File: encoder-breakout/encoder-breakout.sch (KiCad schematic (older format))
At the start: 9 parts, among them J1 Conn_01x06_Female, U1 AEDR-8300

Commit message: Update encoder with 3d footprint
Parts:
- H1, H2: value MountingHole_Pad -> 9774060482R
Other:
- note removed: "TODO: choose correct mounting holes or smd screw receptacle"
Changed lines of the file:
@@
 EESchema Schematic File Version 4
+LIBS:encoder-breakout-cache
 EELAYER 30 0
 EELAYER END
@@
 P 5400 1850
 F 0 "H2" H 5500 1899 50  0000 L CNN
-F 1 "MountingHole_Pad" H 5500 1808 50  0000 L CNN
+F 1 "9774060482R" H 5500 1808 50  0000 L CNN
 F 2 "Jitter_Footprints:MountingHole_M4_threaded_6mm" H 5400 1850 50  0001 C CNN
-F 3 "~" H 5400 1850 50  0001 C CNN
+F 3 "http://www.farnell.com/datasheets/2580475.pdf" H 5400 1850 50  0001 C CNN
 	1    5400 1850
 	1    0    0    -1
@@
 	1    0    0    -1
 $EndComp
-Text Notes 3450 1550 0    79   ~ 0
-TODO: choose correct mounting holes or smd screw receptacle
 $Comp
 L Mechanical:MountingHole_Pad H1
@@
 P 4400 1850
 F 0 "H1" H 4500 1899 50  0000 L CNN
-F 1 "MountingHole_Pad" H 4500 1808 50  0000 L CNN
+F 1 "9774060482R" H 4500 1808 50  0000 L CNN
 F 2 "Jitter_Footprints:MountingHole_M4_threaded_6mm" H 4400 1850 50  0001 C CNN
-F 3 "~" H 4400 1850 50  0001 C CNN
+F 3 "http://www.farnell.com/datasheets/2580475.pdf" H 4400 1850 50  0001 C CNN
 	1    4400 1850
 	1    0    0    -1

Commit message: Add LED MPN information. add power led to UART board
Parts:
- D1: value LED -> KPT-1608EC; Farnell (none) -> 2099221
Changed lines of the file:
@@
 P 8650 1950
 F 0 "D1" V 8689 1833 50  0000 R CNN
-F 1 "LED" V 8598 1833 50  0000 R CNN
+F 1 "KPT-1608EC" V 8598 1833 50  0000 R CNN
 F 2 "LED_SMD:LED_0603_1608Metric" H 8650 1950 50  0001 C CNN
-F 3 "~" H 8650 1950 50  0001 C CNN
+F 3 "http://www.farnell.com/datasheets/2045911.pdf" H 8650 1950 50  0001 C CNN
+F 4 "2099221" V 8650 1950 50  0001 C CNN "Farnell"
 	1    8650 1950
 	0    -1   -1   0

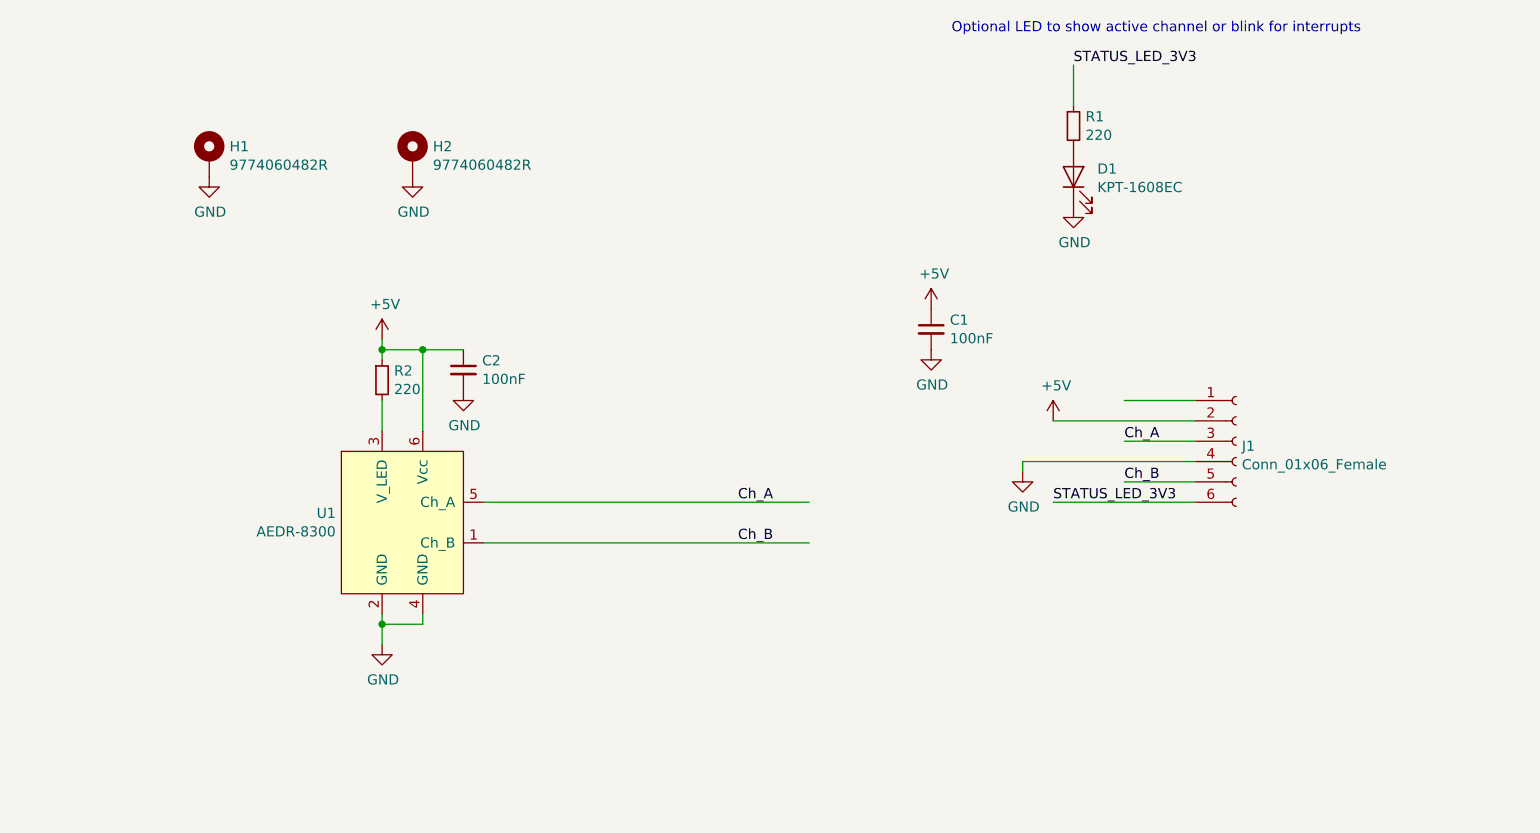
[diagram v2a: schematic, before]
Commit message: Fix schematics compile errors
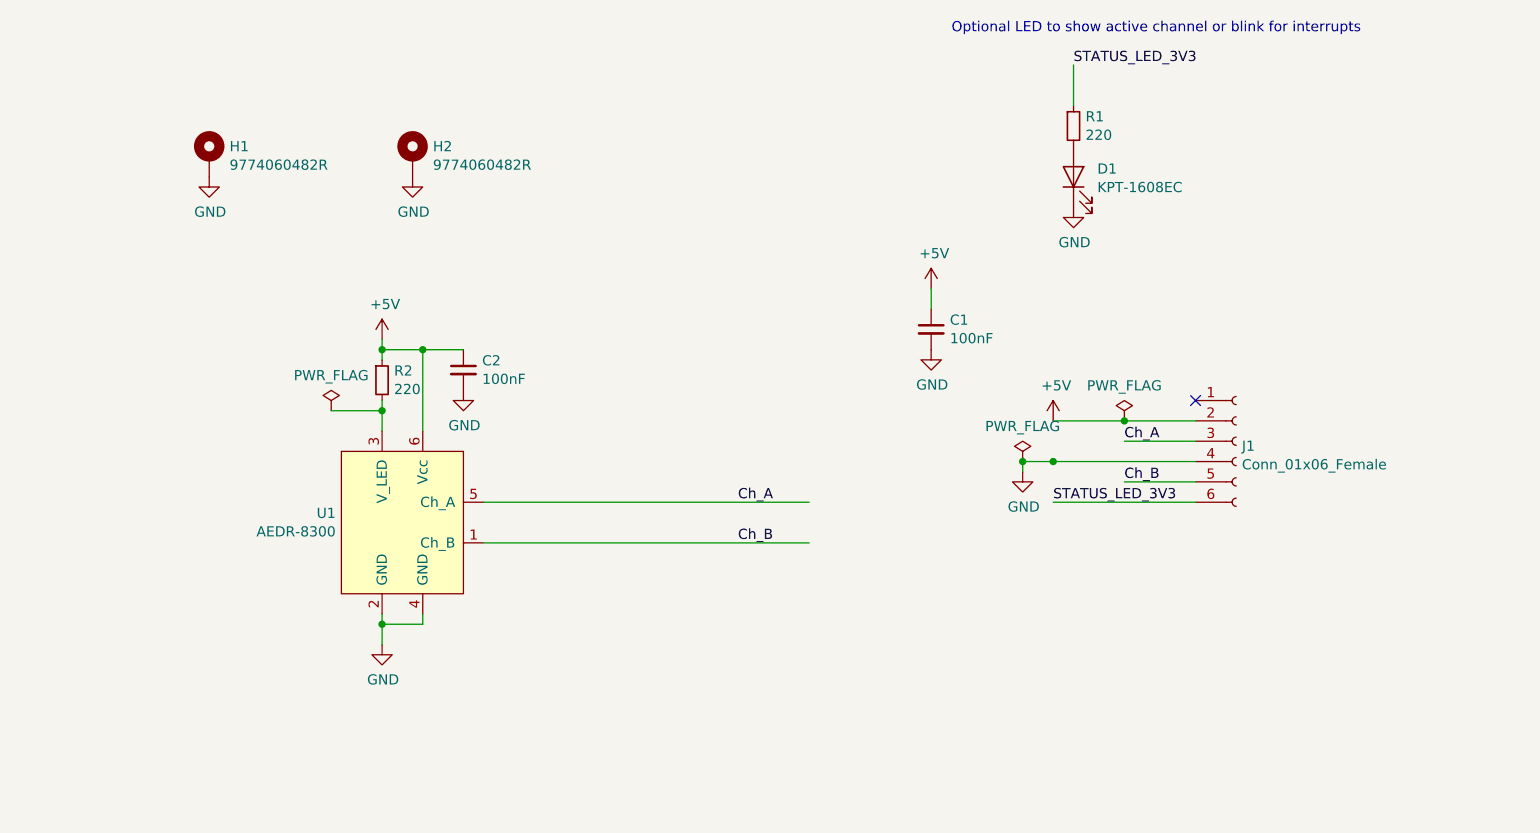
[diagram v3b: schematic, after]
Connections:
- wire segments 20 -> 24
- no-connect marks 0 -> 1
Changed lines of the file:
@@
 $EndComp
 Wire Wire Line
-	5250 3050 5250 3200
+	5250 3050 5250 3100
 $Comp
 L power:+5V #PWR05
@@
 $EndComp
 Wire Wire Line
-	8900 3050 9250 3050
-Wire Wire Line
 	8900 3450 9250 3450
 Wire Wire Line
@@
 L power:+5V #PWR04
 U 1 1 5D93015E
-P 7950 2600
-F 0 "#PWR04" H 7950 2450 50  0001 C CNN
-F 1 "+5V" H 7965 2773 50  0000 C CNN
-F 2 "" H 7950 2600 50  0001 C CNN
-F 3 "" H 7950 2600 50  0001 C CNN
-	1    7950 2600
+P 7950 2500
+F 0 "#PWR04" H 7950 2350 50  0001 C CNN
+F 1 "+5V" H 7965 2673 50  0000 C CNN
+F 2 "" H 7950 2500 50  0001 C CNN
+F 3 "" H 7950 2500 50  0001 C CNN
+	1    7950 2500
 	1    0    0    -1
 $EndComp
@@
 $EndComp
 Wire Wire Line
-	8550 3150 9250 3150
+	8550 3150 8900 3150
 Text Label 8550 3550 0    50   ~ 0
 STATUS_LED_3V3
@@
 	8550 3550 9250 3550
 Wire Wire Line
-	9250 3350 8400 3350
+	9250 3350 8550 3350
 Wire Wire Line
 	8400 3350 8400 3400
+$Comp
+L power:PWR_FLAG #FLG0101
+U 1 1 5D9DAEE1
+P 5000 3100
+F 0 "#FLG0101" H 5000 3175 50  0001 C CNN
+F 1 "PWR_FLAG" H 5000 3273 50  0000 C CNN
+F 2 "" H 5000 3100 50  0001 C CNN
+F 3 "~" H 5000 3100 50  0001 C CNN
+	1    5000 3100
+	1    0    0    -1
+$EndComp
+Wire Wire Line
+	5000 3100 5250 3100
+Connection ~ 5250 3100
+Wire Wire Line
+	5250 3100 5250 3200
+NoConn ~ 9250 3050
+Wire Wire Line
+	7950 2500 7950 2600
+$Comp
+L power:PWR_FLAG #FLG0102
+U 1 1 5D9DD207
+P 8900 3150
+F 0 "#FLG0102" H 8900 3225 50  0001 C CNN
+F 1 "PWR_FLAG" H 8900 3323 50  0000 C CNN
+F 2 "" H 8900 3150 50  0001 C CNN
+F 3 "~" H 8900 3150 50  0001 C CNN
+	1    8900 3150
+	1    0    0    -1
+$EndComp
+Connection ~ 8900 3150
+Wire Wire Line
+	8900 3150 9250 3150
+$Comp
+L power:PWR_FLAG #FLG0103
+U 1 1 5D9DD9D3
+P 8400 3350
+F 0 "#FLG0103" H 8400 3425 50  0001 C CNN
+F 1 "PWR_FLAG" H 8400 3523 50  0000 C CNN
+F 2 "" H 8400 3350 50  0001 C CNN
+F 3 "~" H 8400 3350 50  0001 C CNN
+	1    8400 3350
+	1    0    0    -1
+$EndComp
+Connection ~ 8550 3350
+Wire Wire Line
+	8550 3350 8400 3350
+Connection ~ 8400 3350
 $EndSCHEMATC

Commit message: Encoder breakout V2: sensor was rotated incorrectly!
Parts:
- added LOGO1, LOGO2: DNI, Jitter_Logos:JitterLogo, symbol Jitter_Components:LOGO
- J1: value Conn_01x06_Female -> Conn_01x06_MountingPin; symbol Connector:Conn_01x06_Female -> Connector_Generic_MountingPin:Conn_01x06_MountingPin
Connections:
- wire segments 24 -> 23
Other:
- moved on the sheet: J1
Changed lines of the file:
@@
 Ch_B
 $Comp
-L Connector:Conn_01x06_Female J1
+L Connector_Generic_MountingPin:Conn_01x06_MountingPin J1
 U 1 1 5D92BFA7
 P 9450 3250
 F 0 "J1" H 9478 3226 50  0000 L CNN
-F 1 "Conn_01x06_Female" H 9478 3135 50  0000 L CNN
+F 1 "Conn_01x06_MountingPin" H 9478 3135 50  0000 L CNN
 F 2 "Jitter_Footprints:JST_PH_S6B-PH-SM4-TB_1x06-1MP_P2.00mm_Horizontal" H 9450 3250 50  0001 C CNN
 F 3 "~" H 9450 3250 50  0001 C CNN
@@
 	8550 3550 9250 3550
 Wire Wire Line
-	9250 3350 8550 3350
-Wire Wire Line
 	8400 3350 8400 3400
 $Comp
@@
 	1    0    0    -1
 $EndComp
-Connection ~ 8550 3350
-Wire Wire Line
-	8550 3350 8400 3350
 Connection ~ 8400 3350
+Wire Wire Line
+	8400 3350 9250 3350
+$Comp
+L power:GND #PWR011
+U 1 1 5DB9BB58
+P 9450 3750
+F 0 "#PWR011" H 9450 3500 50  0001 C CNN
+F 1 "GND" H 9455 3577 50  0000 C CNN
+F 2 "" H 9450 3750 50  0001 C CNN
+F 3 "" H 9450 3750 50  0001 C CNN
+	1    9450 3750
+	1    0    0    -1
+$EndComp
+$Comp
+L Jitter_Components:LOGO LOGO2
+U 1 1 5DB9AA77
+P 7500 5000
+F 0 "LOGO2" H 7578 5046 50  0000 L CNN
+F 1 "DNI" H 7578 4955 50  0000 L CNN
+F 2 "Jitter_Logos:JitterLogo" H 7500 5000 50  0001 C CNN
+F 3 "" H 7500 5000 50  0001 C CNN
+	1    7500 5000
+	1    0    0    -1
+$EndComp
+$Comp
+L Jitter_Components:LOGO LOGO1
+U 1 1 5DB9B670
+P 7000 5000
+F 0 "LOGO1" H 7078 5046 50  0000 L CNN
+F 1 "DNI" H 7078 4955 50  0000 L CNN
+F 2 "Jitter_Logos:JitterLogo" H 7000 5000 50  0001 C CNN
+F 3 "" H 7000 5000 50  0001 C CNN
+	1    7000 5000
+	1    0    0    -1
+$EndComp
 $EndSCHEMATC
